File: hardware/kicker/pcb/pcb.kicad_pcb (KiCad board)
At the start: 2 copper layers, 108.7 x 42.8 mm, 35 parts, among them J1 Conn_01x04, J2 Conn_01x04, J3 Conn_01x02, Q1 NMOS, U1 XL6019E1, U2 TS4535TP 250GF 009, U4 TC4427AEOA713_C5804606

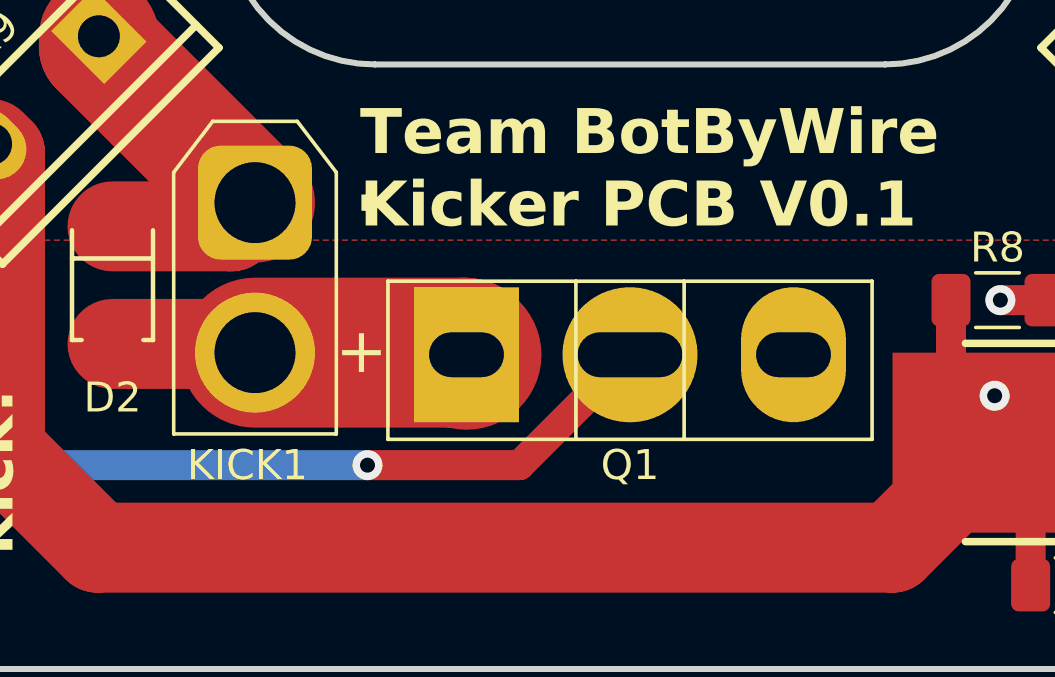
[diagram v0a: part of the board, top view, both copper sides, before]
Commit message: corrected mosfet pinout on kicker pcb (will reorder)
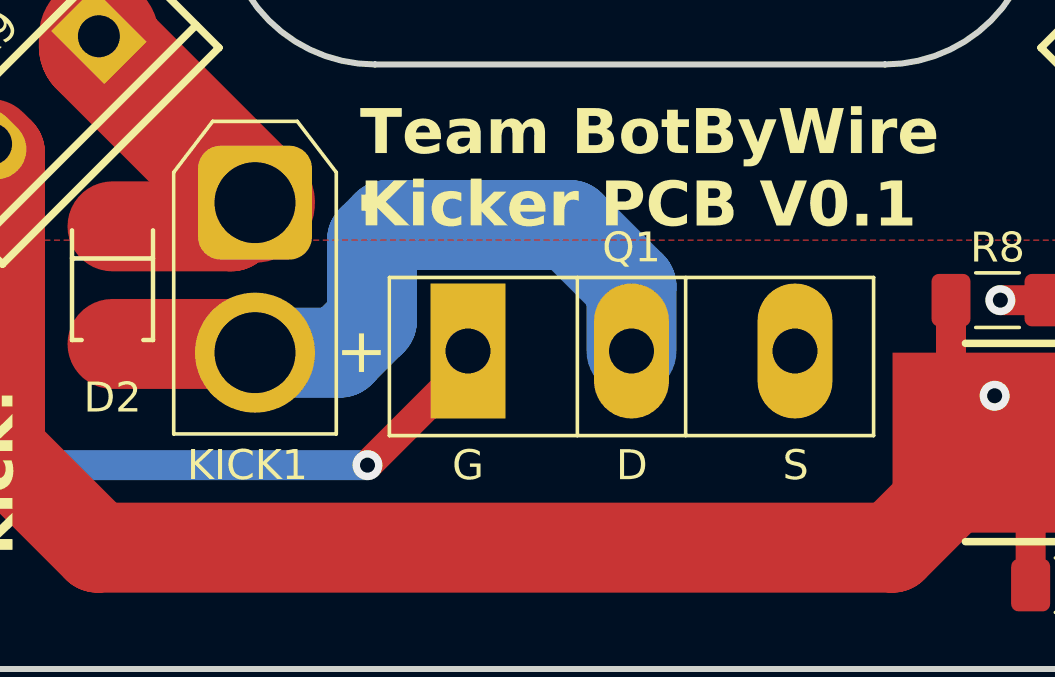
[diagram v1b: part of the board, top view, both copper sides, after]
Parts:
- Q1: value NMOS -> IRFP260N; footprint Package_TO_SOT_THT:TO-247-3_Vertical -> PCM_Package_TO_SOT_THT_AKL:TO-247-3_Vertical_GDS
- moved Q1 0.13 mm to (-5.40, -10.6)
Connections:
- Q1 pad 1: Net-(D2-A) -> /OUTA
- Q1 pad 2: /OUTA -> Net-(D2-A)
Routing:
- net Net-(D2-A): track 11.9 -> 23.8 mm
- net /OUTA: track 39.0 -> 33.9 mm
